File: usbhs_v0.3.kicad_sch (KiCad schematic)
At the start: 65 parts, among them J1 USB_B, J2 Conn_01x02, J3 Conn_01x03, J4 Conn_02x10_Top_Bottom, SW1 SW_Push, SW2 SW_Push, U1 SY8088, U2 USBLC6-2SC6, U3 STM32F446RETx, U4 USB3300-EZK, U5 74LVC1G3157, Y1 12.288M

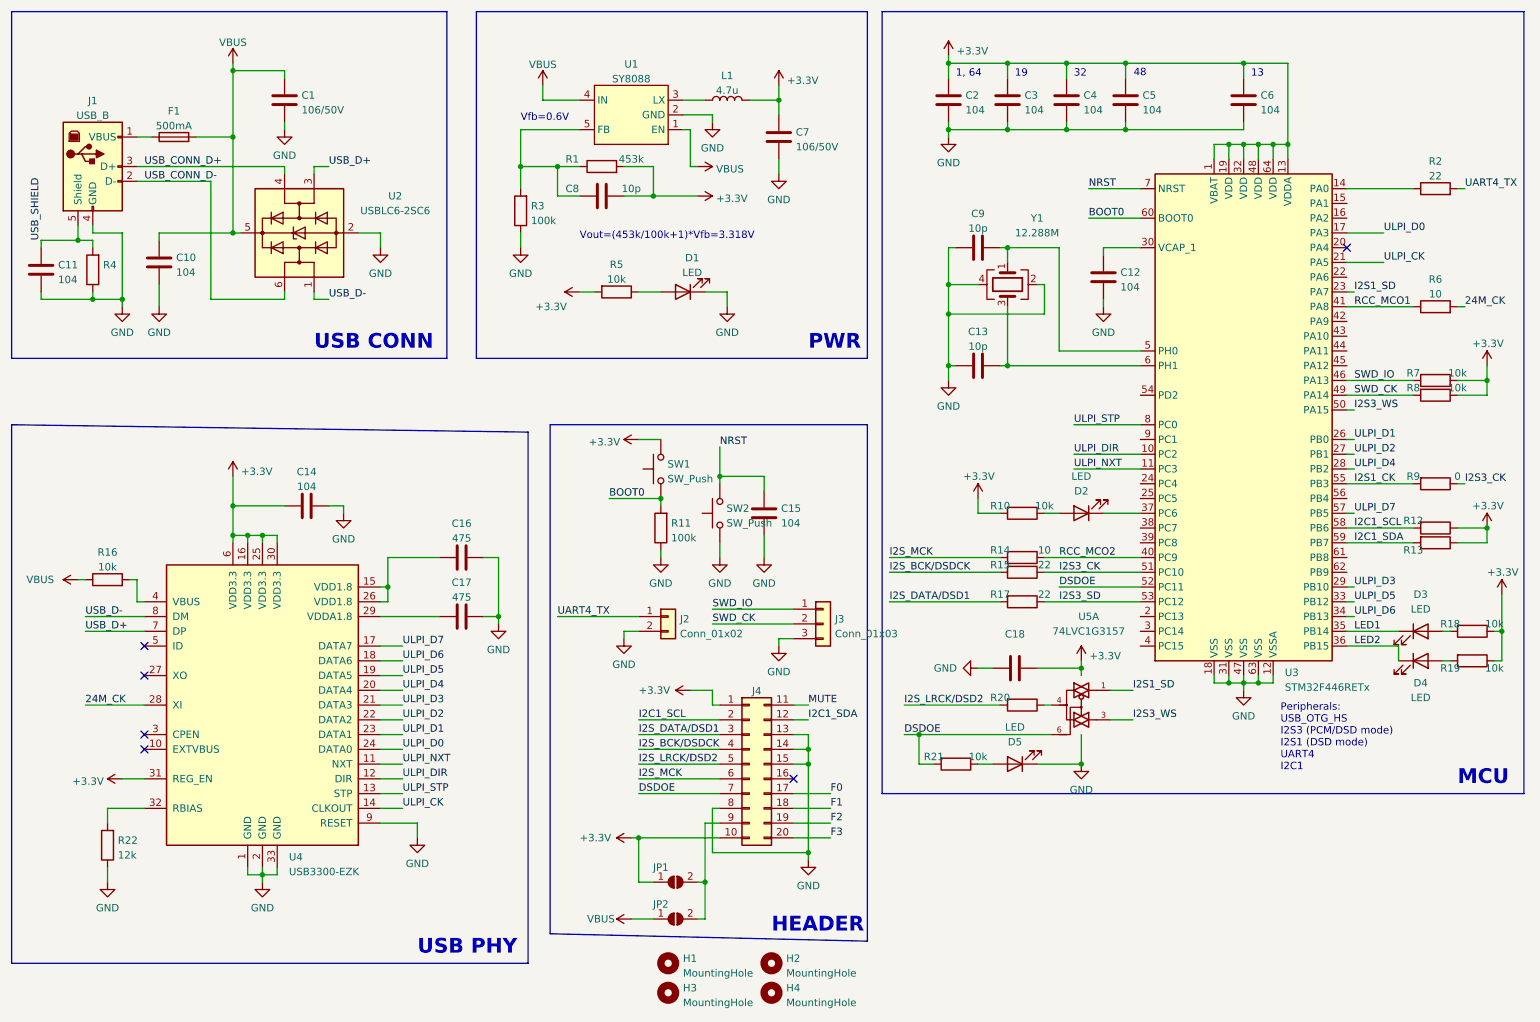
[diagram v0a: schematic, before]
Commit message: modified:   .gitignore 	modified:   usbhs_v0.3.kicad_pcb 	modified:   usbhs_v0.3.kicad_sch 	new file:   usbhs_v0.3.xml
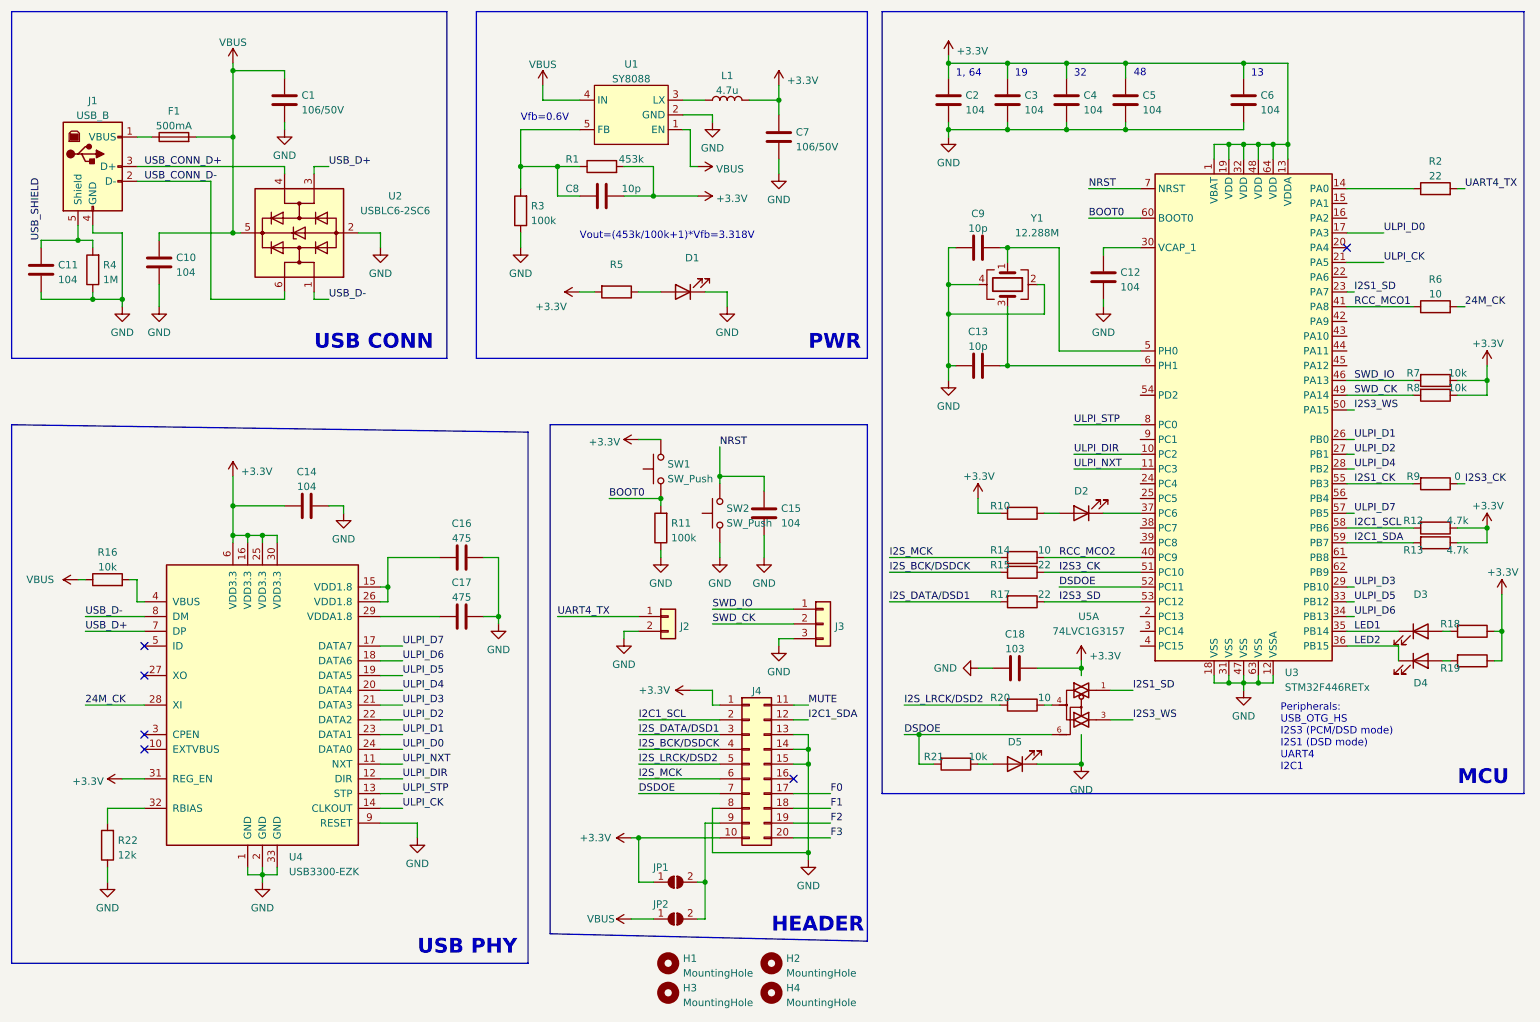
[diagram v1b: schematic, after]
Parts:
- C18: value (none) -> 103
- D1, D2, D3, D4, D5: value LED -> (none); footprint LED_SMD:LED_0603_1608Metric -> (none)
- R10, R18, R19, R5: value 10k -> (none)
- R12, R13: value (none) -> 4.7k
- R20: value (none) -> 10
- R4: value (none) -> 1M
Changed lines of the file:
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@@
     (in_bom yes) (on_board yes)
     (property "Reference" "R10" (id 0) (at 187.96 110.49 90))
-    (property "Value" "10k" (id 1) (at 195.58 110.49 90))
+    (property "Value" "" (id 1) (at 195.58 110.49 90))
     (property "Footprint" "Resistor_SMD:R_0603_1608Metric" (id 2) (at 191.77 109.982 90)
       (effects (font (size 1.27 1.27)) hide)
@@
   (symbol (lib_id "Connector_Generic:Conn_01x03") (at 157.48 130.81 0) (unit 1)
     (in_bom yes) (on_board yes) (fields_autoplaced)
-    (property "Reference" "J3" (id 0) (at 159.512 129.9753 0)
+    (property "Reference" "J3" (id 0) (at 159.512 131.2438 0)
       (effects (font (size 1.27 1.27)) (justify left))
     )
     (property "Value" "Conn_01x03" (id 1) (at 159.512 132.5122 0)
-      (effects (font (size 1.27 1.27)) (justify left))
+      (effects (font (size 1.27 1.27)) (justify left) hide)
     )
     (property "Footprint" "Connector_PinHeader_2.54mm:PinHeader_1x03_P2.54mm_Vertical" (id 2) (at 157.48 130.81 0)
@@
   (symbol (lib_id "Connector_Generic:Conn_01x02") (at 130.81 129.54 0) (unit 1)
     (in_bom yes) (on_board yes) (fields_autoplaced)
-    (property "Reference" "J2" (id 0) (at 132.842 129.9753 0)
+    (property "Reference" "J2" (id 0) (at 132.842 131.2438 0)
       (effects (font (size 1.27 1.27)) (justify left))
     )
     (property "Value" "Conn_01x02" (id 1) (at 132.842 132.5122 0)
-      (effects (font (size 1.27 1.27)) (justify left))
+      (effects (font (size 1.27 1.27)) (justify left) hide)
     )
     (property "Footprint" "Connector_PinHeader_2.54mm:PinHeader_1x02_P2.54mm_Vertical" (id 2) (at 130.81 129.54 0)
@@
     (in_bom yes) (on_board yes) (fields_autoplaced)
     (property "Reference" "D1" (id 0) (at 134.9375 67.8012 0))
-    (property "Value" "LED" (id 1) (at 134.9375 70.3381 0))
-    (property "Footprint" "LED_SMD:LED_0603_1608Metric" (id 2) (at 133.35 73.66 0)
+    (property "Value" "" (id 1) (at 134.9375 70.3381 0))
+    (property "Footprint" "" (id 2) (at 133.35 73.66 0)
       (effects (font (size 1.27 1.27)) hide)
     )
@@
     (in_bom yes) (on_board yes)
     (property "Reference" "R19" (id 0) (at 265.43 138.43 90))
-    (property "Value" "10k" (id 1) (at 273.05 138.43 90))
+    (property "Value" "" (id 1) (at 273.05 138.43 90))
     (property "Footprint" "Resistor_SMD:R_0603_1608Metric" (id 2) (at 269.24 135.382 90)
       (effects (font (size 1.27 1.27)) hide)
@@
     (in_bom yes) (on_board yes)
     (property "Reference" "D2" (id 0) (at 201.93 107.9469 0))
-    (property "Value" "LED" (id 1) (at 201.93 105.41 0))
-    (property "Footprint" "LED_SMD:LED_0603_1608Metric" (id 2) (at 201.93 111.76 0)
+    (property "Value" "" (id 1) (at 201.93 105.41 0))
+    (property "Footprint" "" (id 2) (at 201.93 111.76 0)
       (effects (font (size 1.27 1.27)) hide)
     )
@@
     (in_bom yes) (on_board yes)
     (property "Reference" "D5" (id 0) (at 190.5 151.1269 0))
-    (property "Value" "LED" (id 1) (at 190.5 148.59 0))
-    (property "Footprint" "LED_SMD:LED_0603_1608Metric" (id 2) (at 190.5 154.94 0)
+    (property "Value" "" (id 1) (at 190.5 148.59 0))
+    (property "Footprint" "" (id 2) (at 190.5 154.94 0)
       (effects (font (size 1.27 1.27)) hide)
     )
@@
     (in_bom yes) (on_board yes)
     (property "Reference" "R13" (id 0) (at 259.08 118.11 90))
-    (property "Value" "" (id 1) (at 266.7 118.11 90))
+    (property "Value" "4.7k" (id 1) (at 266.7 118.11 90))
     (property "Footprint" "Resistor_SMD:R_0603_1608Metric" (id 2) (at 262.89 115.062 90)
       (effects (font (size 1.27 1.27)) hide)
@@
     (in_bom yes) (on_board yes)
     (property "Reference" "R18" (id 0) (at 265.43 130.81 90))
-    (property "Value" "10k" (id 1) (at 273.05 130.81 90))
+    (property "Value" "" (id 1) (at 273.05 130.81 90))
     (property "Footprint" "Resistor_SMD:R_0603_1608Metric" (id 2) (at 269.24 130.302 90)
       (effects (font (size 1.27 1.27)) hide)
@@
       (effects (font (size 1.27 1.27)) (justify right))
     )
-    (property "Value" "" (id 1) (at 33.528 71.5522 0)
+    (property "Value" "1M" (id 1) (at 33.528 71.5522 0)
       (effects (font (size 1.27 1.27)) (justify right))
     )
@@
     (in_bom yes) (on_board yes) (fields_autoplaced)
     (property "Reference" "R5" (id 0) (at 121.92 68.9442 90))
-    (property "Value" "10k" (id 1) (at 121.92 71.4811 90))
+    (property "Value" "" (id 1) (at 121.92 71.4811 90))
     (property "Footprint" "Resistor_SMD:R_0603_1608Metric" (id 2) (at 121.92 71.882 90)
       (effects (font (size 1.27 1.27)) hide)
@@
     (in_bom yes) (on_board yes)
     (property "Reference" "D4" (id 0) (at 260.35 140.9731 0))
-    (property "Value" "LED" (id 1) (at 260.35 143.51 0))
-    (property "Footprint" "LED_SMD:LED_0603_1608Metric" (id 2) (at 260.35 137.16 0)
+    (property "Value" "" (id 1) (at 260.35 143.51 0))
+    (property "Footprint" "" (id 2) (at 260.35 137.16 0)
       (effects (font (size 1.27 1.27)) hide)
     )
@@
     (in_bom yes) (on_board yes)
     (property "Reference" "R12" (id 0) (at 259.08 113.03 90))
-    (property "Value" "" (id 1) (at 266.7 113.03 90))
+    (property "Value" "4.7k" (id 1) (at 266.7 113.03 90))
     (property "Footprint" "Resistor_SMD:R_0603_1608Metric" (id 2) (at 262.89 112.522 90)
       (effects (font (size 1.27 1.27)) hide)
@@
     (in_bom yes) (on_board yes)
     (property "Reference" "R20" (id 0) (at 187.96 143.51 90))
-    (property "Value" "" (id 1) (at 195.58 143.51 90))
+    (property "Value" "10" (id 1) (at 195.58 143.51 90))
     (property "Footprint" "Resistor_SMD:R_0603_1608Metric" (id 2) (at 191.77 143.002 90)
       (effects (font (size 1.27 1.27)) hide)
@@
     (in_bom yes) (on_board yes) (fields_autoplaced)
     (property "Reference" "C18" (id 0) (at 190.5 132.5712 90))
-    (property "Value" "" (id 1) (at 190.5 135.1081 90))
+    (property "Value" "103" (id 1) (at 190.5 135.1081 90))
     (property "Footprint" "Capacitor_SMD:C_0603_1608Metric" (id 2) (at 186.69 139.3952 0)
       (effects (font (size 1.27 1.27)) hide)
@@
     (in_bom yes) (on_board yes)
     (property "Reference" "D3" (id 0) (at 260.35 125.7331 0))
-    (property "Value" "LED" (id 1) (at 260.35 128.27 0))
-    (property "Footprint" "LED_SMD:LED_0603_1608Metric" (id 2) (at 260.35 132.08 0)
+    (property "Value" "" (id 1) (at 260.35 128.27 0))
+    (property "Footprint" "" (id 2) (at 260.35 132.08 0)
       (effects (font (size 1.27 1.27)) hide)
     )
@@
     )
     (path "/47fb8d06-9abf-4836-a22b-0ed5cd446d51"
-      (reference "D1") (unit 1) (value "LED") (footprint "LED_SMD:LED_0603_1608Metric")
+      (reference "D1") (unit 1) (value "LED_WHITE") (footprint "LED_SMD:LED_0603_1608Metric")
     )
     (path "/6e0136e8-1617-4596-937b-333822c8faa8"
-      (reference "D2") (unit 1) (value "LED") (footprint "LED_SMD:LED_0603_1608Metric")
+      (reference "D2") (unit 1) (value "LED_BLUE") (footprint "LED_SMD:LED_0603_1608Metric")
     )
     (path "/ef38983d-1e95-4444-bbe5-be509f249cde"
-      (reference "D3") (unit 1) (value "LED") (footprint "LED_SMD:LED_0603_1608Metric")
+      (reference "D3") (unit 1) (value "LED_RED") (footprint "LED_SMD:LED_0603_1608Metric")
     )
     (path "/e17c40ef-dd99-47ff-9785-6c1ad4aa93a9"
-      (reference "D4") (unit 1) (value "LED") (footprint "LED_SMD:LED_0603_1608Metric")
+      (reference "D4") (unit 1) (value "LED_GREEN") (footprint "LED_SMD:LED_0603_1608Metric")
     )
     (path "/821483bf-9f7e-4649-86e1-c234c345bc5b"
-      (reference "D5") (unit 1) (value "LED") (footprint "LED_SMD:LED_0603_1608Metric")
+      (reference "D5") (unit 1) (value "LED_YELLOW") (footprint "LED_SMD:LED_0603_1608Metric")
     )
     (path "/9f99d8bd-86c8-4cd3-87e8-674bf81ec7da"
@@
     )
     (path "/cb712688-5299-4cd7-b82a-14a07c3ba87b"
-      (reference "R5") (unit 1) (value "10k") (footprint "Resistor_SMD:R_0603_1608Metric")
+      (reference "R5") (unit 1) (value "1k") (footprint "Resistor_SMD:R_0603_1608Metric")
     )
     (path "/9063b0a8-3226-4a61-a899-3707e9b8a619"
@@
     )
     (path "/07244beb-ead2-4da3-b999-697f3b020a65"
-      (reference "R10") (unit 1) (value "10k") (footprint "Resistor_SMD:R_0603_1608Metric")
+      (reference "R10") (unit 1) (value "1k") (footprint "Resistor_SMD:R_0603_1608Metric")
     )
     (path "/3f4fc8f5-ea24-4ea0-8ee3-a10851cd8c01"
@@
     )
     (path "/bde8bde3-80fb-478e-8404-88041cc5eb54"
-      (reference "R18") (unit 1) (value "10k") (footprint "Resistor_SMD:R_0603_1608Metric")
+      (reference "R18") (unit 1) (value "1k") (footprint "Resistor_SMD:R_0603_1608Metric")
     )
     (path "/5233cf4e-69e7-46dd-a8d0-4d4f190557d1"
-      (reference "R19") (unit 1) (value "10k") (footprint "Resistor_SMD:R_0603_1608Metric")
+      (reference "R19") (unit 1) (value "1k") (footprint "Resistor_SMD:R_0603_1608Metric")
     )
     (path "/e55b7901-0800-4f58-8579-30231bcbcd60"

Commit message: modified:   .gitignore 	modified:   usbhs_v0.3.kicad_pcb 	modified:   usbhs_v0.3.kicad_sch 	deleted:    usbhs_v0.3.xml
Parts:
- removed C13, C9: 10p, Capacitor_SMD:C_0603_1608Metric, symbol Device:C
- removed Y1: 12.288M, Crystal:Crystal_SMD_3225-4Pin_3.2x2.5mm, symbol Device:Crystal_GND24
- added C12: 103, Capacitor_SMD:C_0603_1608Metric, symbol Device:C
- added FB1: 600R, Inductor_SMD:L_0603_1608Metric, symbol Device:FerriteBead
- added X1: 24.576M, Crystal:Crystal_SMD_3225-4Pin_3.2x2.5mm, symbol Oscillator:XO32
- D1: value (none) -> LED_WHITE; footprint (none) -> LED_SMD:LED_0603_1608Metric
- D2: value (none) -> LED_BLUE; footprint (none) -> LED_SMD:LED_0603_1608Metric
- D3: value (none) -> LED_RED; footprint (none) -> LED_SMD:LED_0603_1608Metric
- D4: value (none) -> LED_GREEN; footprint (none) -> LED_SMD:LED_0603_1608Metric
- D5: value (none) -> LED_YELLOW; footprint (none) -> LED_SMD:LED_0603_1608Metric
- R10, R18, R19, R5: value (none) -> 1k
- R21: value 10k -> (none); footprint Resistor_SMD:R_0603_1608Metric -> (none)
- renumbered C11 to C10, C12 to C11, C14 to C13, C15 to C14, C16 to C15, C17 to C16, C18 to C17, C10 to C9
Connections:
- net +3V3: now also FB1.1
- net GND: now also C12.1, X1.2 (GND)
- net at U3.5 (PH0): now also X1.3 (OUT)
- new net: C12.2, FB1.2, X1.1 (EN), X1.4 (V+)
- no-connect marks 6 -> 7

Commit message: modified:   usbhs_v0.3.kicad_pcb 	modified:   usbhs_v0.3.kicad_sch
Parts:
- added R8: (no value), Resistor_SMD:R_0603_1608Metric, symbol Device:R
- R22: renamed from R21; value (none) -> 1k; footprint (none) -> Resistor_SMD:R_0603_1608Metric
- renumbered R9 to R10, R10 to R11, R11 to R12, R12 to R13, R13 to R14, R14 to R15, R15 to R16, R16 to R17, R17 to R18, R18 to R19, R19 to R20, R20 to R21, R22 to R23, R8 to R9
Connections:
- net I2S3_WS: now also R8.2
- net MUTE: now also U3.61 (PB8)
- net EXTI2: now reaches U3.54 (PD2)
- net EXTI2: now also R8.1
